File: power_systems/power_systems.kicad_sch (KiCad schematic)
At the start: 13 parts, among them J1 Screw_Terminal_01x02, J2 Screw_Terminal_01x02, J3 Screw_Terminal_01x02, U1 LM2576HVS-5, U2 LM2576HVS-12

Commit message: Rev2 schematic changes
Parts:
- removed D2: D_Schottky, Diode_SMD:D_0201_0603Metric, symbol Device:D_Schottky
- removed U2: LM2576HVS-12, Package_TO_SOT_SMD:TO-263-5_TabPin3, symbol Regulator_Switching:LM2576HVS-12
- added C10, C14: 24 pF, Capacitor_SMD:CP_Elec_4x3, symbol Device:C
- added C11: 5 uF, Capacitor_SMD:CP_Elec_4x3, symbol Device:C
- added C12, C16, C5, C8: 100 nF, Capacitor_SMD:CP_Elec_4x3, symbol Device:C
- added C13, C9: 820 pF, Capacitor_SMD:CP_Elec_4x3, symbol Device:C
- added C15, C6: 2.2 uF, Capacitor_SMD:CP_Elec_4x3, symbol Device:C
- added C7: 10 uF, Capacitor_SMD:CP_Elec_4x3, symbol Device:C
- added J4: Screw_Terminal_24V, TerminalBlock:TerminalBlock_MaiXu_MX126-5.0-02P_1x02_P5.00mm, symbol Connector:Screw_Terminal_01x02
- added J5: Screw_Terminal_GPIO, TerminalBlock_4Ucon:TerminalBlock_4Ucon_1x03_P3.50mm_Horizontal, symbol Connector:Screw_Terminal_01x03
- added J6: Screw_Terminal_V1, TerminalBlock_4Ucon:TerminalBlock_4Ucon_1x02_P3.50mm_Vertical, symbol Connector:Screw_Terminal_01x02
- added J7: Screw_Terminal_V2, TerminalBlock_4Ucon:TerminalBlock_4Ucon_1x02_P3.50mm_Vertical, symbol Connector:Screw_Terminal_01x02
- added J8: Screw_Terminal_V3, TerminalBlock_4Ucon:TerminalBlock_4Ucon_1x02_P3.50mm_Vertical, symbol Connector:Screw_Terminal_01x02
- added L3: 1.2 uH, Inductor_SMD:L_7.3x7.3_H3.5, symbol Device:L
- added Q1, Q2, Q3, Q4, Q6, Q7, Q8: CSD18534Q5A, Package_TO_SOT_SMD:TDSON-8-1, symbol Transistor_FET:CSD18534Q5A
- added R1, R8: 7mOhm, Resistor_SMD:R_0201_0603Metric, symbol Device:R_US
- added R10: 29kOhm, Resistor_SMD:R_0201_0603Metric, symbol Device:R_US
- added R11: 1kOhm, Resistor_SMD:R_0201_0603Metric, symbol Device:R_US
- added R12, R7: 5.6kOhm, Resistor_SMD:R_0201_0603Metric, symbol Device:R_US
- added R13, R4: 9.53kOhm, Resistor_SMD:R_0201_0603Metric, symbol Device:R_US
- added R14, R5: 40.2kOhm, Resistor_SMD:R_0201_0603Metric, symbol Device:R_US
- added R2: 82.5kOhm, Resistor_SMD:R_0201_0603Metric, symbol Device:R_US
- added R3: 10kOhm, Resistor_SMD:R_0201_0603Metric, symbol Device:R_US
- added R6, R9: 100 kOhm, Resistor_SMD:R_0201_0603Metric, symbol Device:R_US
- added U2, U3: ~, footprints:RGY0024F-MFG, symbol LM5148:LM5148
- C3: value C -> 5 uF
- C4: value 100 uF -> 10 uF
- J2: value Screw_Terminal_01x02 -> Screw_Terminal_5V
- J3: value Screw_Terminal_01x02 -> Screw_Terminal_7.4V
- L2: value L -> 1.2 uH
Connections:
- net GND: now also C10.1, C11.2, C13.1, C14.1, C15.2, C16.2, C6.2, C7.2, C8.2, C9.1, J4.2 (Pin_2), J6.2 (Pin_2), J7.2 (Pin_2), J8.2 (Pin_2), Q2.1 (S), Q2.2 (S), Q2.3 (S), Q4.1 (S), Q4.2 (S), Q4.3 (S), R11.2, R13.2, R14.2, R3.2, R4.2, R5.2, R6.1, R9.1, U2.10 (PGND), U2.16 (VCCX), U2.7 (AGND), U3.10 (PGND), U3.16 (VCCX), U3.7 (AGND)
- net +BATT: now reaches C1.2, J1.2 (Pin_2), U1.1 (VIN)
- net +BATT: now also C3.1, C11.1, Q1.5 (D), Q3.5 (D), U2.12 (VIN), U2.19 (EN), U3.12 (VIN), U3.19 (EN); no longer C4.1
- net at L2.1: now also R1.2, U2.20 (ISNS+)
- new net: C5.1, L2.2, Q1.1 (S), Q1.2 (S), Q1.3 (S), Q2.5 (D), U2.14 (SW)
- new net: J7.1 (Pin_1), Q7.1 (S), Q7.2 (S), Q7.3 (S)
- new net: J5.2 (Pin_2), Q7.4 (G)
- new net: R4.1, U2.4 (RT)
- new net: C10.2, R7.2, U2.5 (EXTCOMP)
- new net: R13.1, U3.4 (RT)
- new net: L3.1, R8.2, U3.20 (ISNS+)
- new net: C4.1, J3.1 (Pin_1), R1.1, R2.1, U2.21 (VOUT)
- new net: J8.1 (Pin_1), Q8.1 (S), Q8.2 (S), Q8.3 (S)
- new net: Q4.4 (G), U3.11 (LO)
- new net: Q3.4 (G), U3.13 (HO)
- new net: C12.1, L3.2, Q3.1 (S), Q3.2 (S), Q3.3 (S), Q4.5 (D), U3.14 (SW)
- new net: C12.2, U3.15 (CBOOT)
- new net: R9.2, U3.17 (PG/SYNCOUT)
- new net: R14.1, U3.3 (CNFG)
- new net: C14.2, R12.2, U3.5 (EXTCOMP)
- new net: C15.1, U3.9 (VCC)
- new net: J5.1 (Pin_1), Q8.4 (G)
- new net: J5.3 (Pin_3), Q6.4 (G)
- new net: J6.1 (Pin_1), Q6.1 (S), Q6.2 (S), Q6.3 (S)
- new net: Q2.4 (G), U2.11 (LO)
- new net: Q1.4 (G), U2.13 (HO)
- new net: C5.2, U2.15 (CBOOT)
- new net: R6.2, U2.17 (PG/SYNCOUT)
- new net: R5.1, U2.3 (CNFG)
- new net: C6.1, U2.9 (VCC)
- new net: C13.2, R12.1
- new net: C9.2, R7.1
- new net +24V: C7.1, J4.1 (Pin_1), Q6.5 (D), Q7.5 (D), Q8.5 (D), R10.1, R8.1, U3.21 (VOUT)
- new net VDDA_24: C16.1, U3.18 (PFM/SYNC), U3.8 (VDDA)
- new net VDDA_7.4: C8.1, U2.18 (PFM/SYNC), U2.8 (VDDA)
- new net V_FB_24: R10.2, R11.1, U3.6 (FB)
- new net V_FB_7.4: R2.2, R3.1, U2.6 (FB)
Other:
- note added: "24V"
- note added: "5V"
- note added: "7.4V"
- note added: "Valve Control"
- moved on the sheet: C1, C2, D1, J1, J2, L1, U1

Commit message: power systems update and fc redesign
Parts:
- removed C1: 100 uF, Capacitor_SMD:CP_Elec_4x3, symbol Device:C
- removed C10, C14: 24 pF, Capacitor_SMD:CP_Elec_4x3, symbol Device:C
- removed C11, C3: 5 uF, Capacitor_SMD:CP_Elec_4x3, symbol Device:C
- removed C12, C16, C5, C8: 100 nF, Capacitor_SMD:CP_Elec_4x3, symbol Device:C
- removed C13, C9: 820 pF, Capacitor_SMD:CP_Elec_4x3, symbol Device:C
- removed C15, C6: 2.2 uF, Capacitor_SMD:CP_Elec_4x3, symbol Device:C
- removed C2: 1000 uF, Capacitor_SMD:CP_Elec_4x3, symbol Device:C
- removed C4, C7: 10 uF, Capacitor_SMD:CP_Elec_4x3, symbol Device:C
- removed D1: D_Schottky, Diode_SMD:D_0201_0603Metric, symbol Device:D_Schottky
- removed J1: Screw_Terminal_01x02, TerminalBlock:TerminalBlock_MaiXu_MX126-5.0-02P_1x02_P5.00mm, symbol Connector:Screw_Terminal_01x02
- removed J2: Screw_Terminal_5V, TerminalBlock:TerminalBlock_MaiXu_MX126-5.0-02P_1x02_P5.00mm, symbol Connector:Screw_Terminal_01x02
- removed J3: Screw_Terminal_7.4V, TerminalBlock:TerminalBlock_MaiXu_MX126-5.0-02P_1x02_P5.00mm, symbol Connector:Screw_Terminal_01x02
- removed J4: Screw_Terminal_24V, TerminalBlock:TerminalBlock_MaiXu_MX126-5.0-02P_1x02_P5.00mm, symbol Connector:Screw_Terminal_01x02
- removed J5: Screw_Terminal_GPIO, TerminalBlock_4Ucon:TerminalBlock_4Ucon_1x03_P3.50mm_Horizontal, symbol Connector:Screw_Terminal_01x03
- removed J6: Screw_Terminal_V1, TerminalBlock_4Ucon:TerminalBlock_4Ucon_1x02_P3.50mm_Vertical, symbol Connector:Screw_Terminal_01x02
- removed J7: Screw_Terminal_V2, TerminalBlock_4Ucon:TerminalBlock_4Ucon_1x02_P3.50mm_Vertical, symbol Connector:Screw_Terminal_01x02
- removed J8: Screw_Terminal_V3, TerminalBlock_4Ucon:TerminalBlock_4Ucon_1x02_P3.50mm_Vertical, symbol Connector:Screw_Terminal_01x02
- removed L1: 100 uH, Inductor_SMD:L_7.3x7.3_H3.5, symbol Device:L
- removed L2, L3: 1.2 uH, Inductor_SMD:L_7.3x7.3_H3.5, symbol Device:L
- removed Q1, Q2, Q3, Q4, Q6, Q7, Q8: CSD18534Q5A, Package_TO_SOT_SMD:TDSON-8-1, symbol Transistor_FET:CSD18534Q5A
- removed R1, R8: 7mOhm, Resistor_SMD:R_0201_0603Metric, symbol Device:R_US
- removed R10: 29kOhm, Resistor_SMD:R_0201_0603Metric, symbol Device:R_US
- removed R11: 1kOhm, Resistor_SMD:R_0201_0603Metric, symbol Device:R_US
- removed R12, R7: 5.6kOhm, Resistor_SMD:R_0201_0603Metric, symbol Device:R_US
- removed R13, R4: 9.53kOhm, Resistor_SMD:R_0201_0603Metric, symbol Device:R_US
- removed R14, R5: 40.2kOhm, Resistor_SMD:R_0201_0603Metric, symbol Device:R_US
- removed R2: 82.5kOhm, Resistor_SMD:R_0201_0603Metric, symbol Device:R_US
- removed R3: 10kOhm, Resistor_SMD:R_0201_0603Metric, symbol Device:R_US
- removed R6, R9: 100 kOhm, Resistor_SMD:R_0201_0603Metric, symbol Device:R_US
- removed U1: LM2576HVS-5, Package_TO_SOT_SMD:TO-263-5_TabPin3, symbol Regulator_Switching:LM2576HVS-5
- removed U2, U3: ~, footprints:RGY0024F-MFG, symbol LM5148:LM5148
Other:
- added sheet battery_step_down (battery_step_down.kicad_sch)
- note removed: "24V"
- note removed: "5V"
- note removed: "7.4V"
- note removed: "Valve Control"

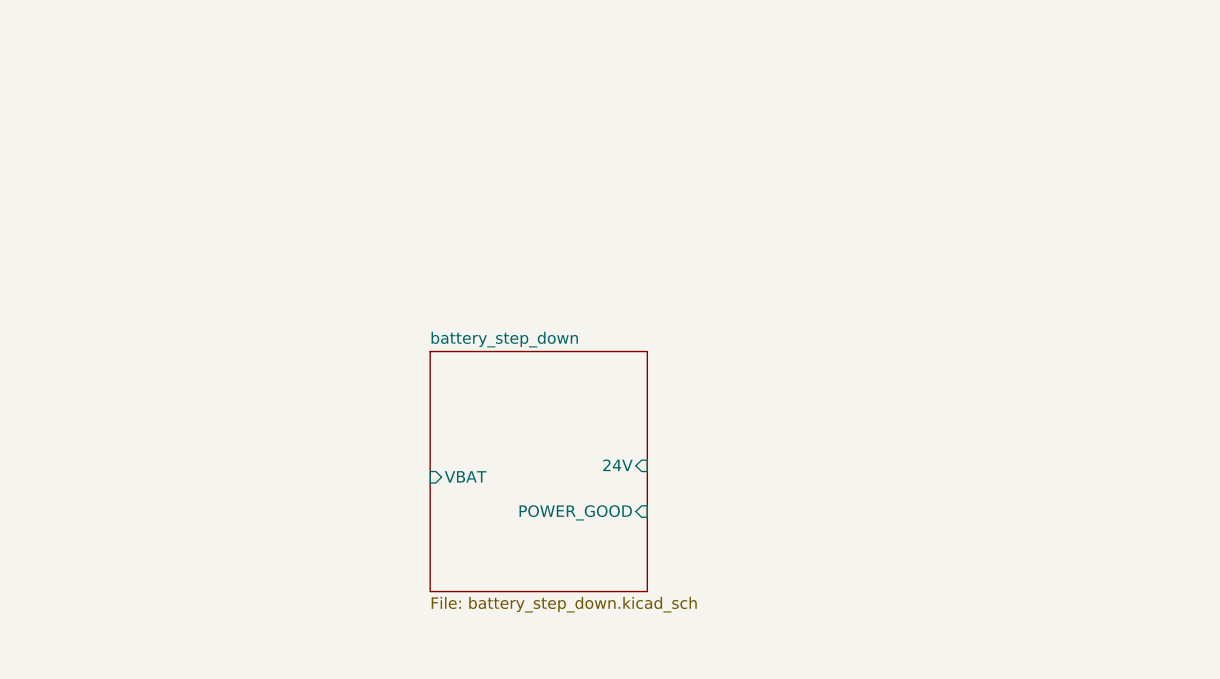
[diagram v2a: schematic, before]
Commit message: Schematics and layouting for power systems board
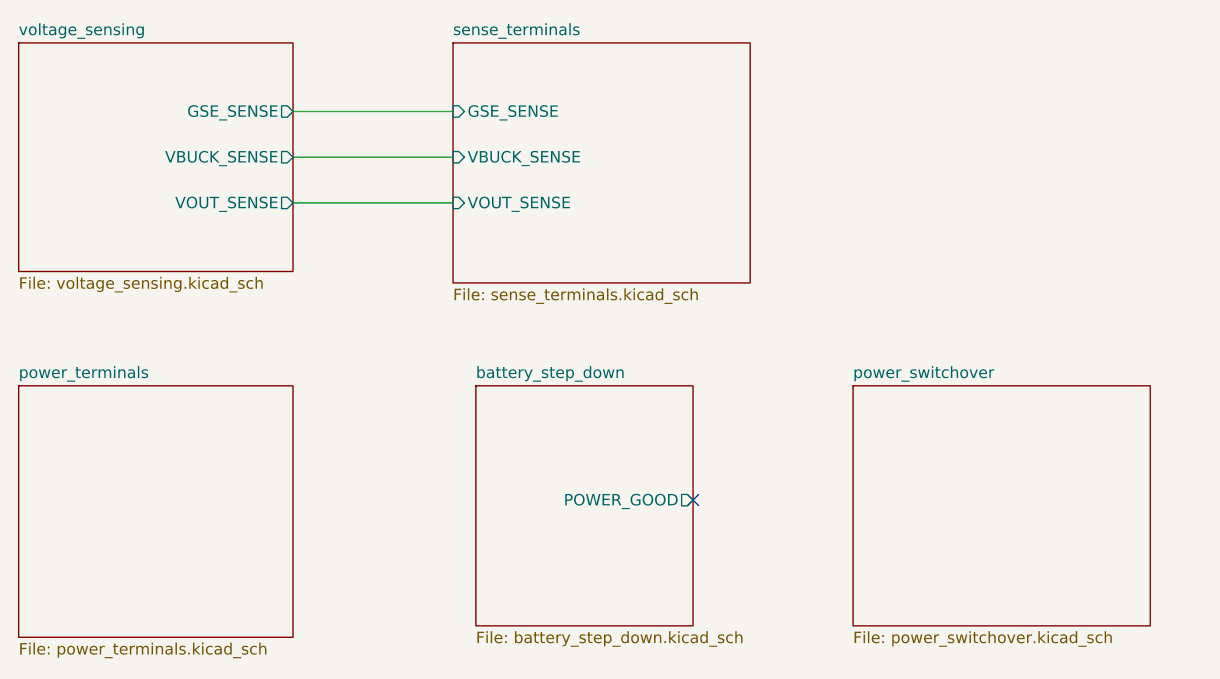
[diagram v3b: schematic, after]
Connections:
- no-connect marks 0 -> 1
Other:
- added sheet power_switchover (power_switchover.kicad_sch)
- added sheet power_terminals (power_terminals.kicad_sch)
- added sheet sense_terminals (sense_terminals.kicad_sch)
- added sheet voltage_sensing (voltage_sensing.kicad_sch)
- sheet battery_step_down ports: added none; removed 24V, VBAT

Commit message: Power systems routing v1
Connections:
- no-connect marks 1 -> 0
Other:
- sheet power_terminals renamed input_power_terminals
- removed sheet sense_terminals
- added sheet output_power_terminals (output_power_terminals.kicad_sch)
- sheet battery_step_down ports: added +BATT, +VBUCK; removed POWER_GOOD
- sheet input_power_terminals ports: added +BATT, +GSE; removed none
- sheet power_switchover ports: added +GSE, +VBUCK, +VOUT; removed none
- sheet voltage_sensing ports: added +GSE, +VBUCK, +VOUT; removed none
